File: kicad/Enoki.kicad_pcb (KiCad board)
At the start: 2 copper layers, 40 x 23 mm, 16 parts, among them J1 Conn_01x08_Male

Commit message: save
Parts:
- DS1: footprint Display:OLED-128O064D -> allen-synthesis:KH-FPC0.5-H2.0SMT-30P-QCH FPC Connector 30 pin
- R4: value 390K -> 330K
- moved DS1 4.60 mm to (137.2, 158.8), turned to 0 degrees
- moved C3 0.80 mm to (126.7, 151.4)
- moved C1 0.76 mm to (128.8, 149.0)
- moved C2 0.70 mm to (145.4, 149.0)
- moved C4 0.70 mm to (147.3, 151.4)
- moved C5 0.70 mm to (143.3, 151.4)
- moved R1 0.64 mm to (140.3, 150.2)
- moved C6 0.63 mm to (130.8, 151.4)
- moved R4 0.63 mm to (133.9, 150.2)
- moved JP1 0.38 mm to (151.1, 151.1)
- moved R3 0.25 mm to (136.0, 150.2)
- moved R2 0.13 mm to (138.2, 150.2)
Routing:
- net GND: track 28.0 -> 15.0 mm, vias 6 -> 8
- net /D0/SCLK/SCK_3.3V: track 21.3 -> 13.1 mm, vias 2 -> 0
- net +3V3: track 53.5 -> 60.3 mm, vias 3 -> 2
- net /RST_3.3V: track 8.62 -> 14.4 mm
- net Net-(DS1-C2N): track 3.22 -> 6.56 mm
- net Net-(DS1-VCC): track 2.86 -> 5.65 mm
- net Net-(DS1-C2P): track 2.86 -> 5.55 mm
- net Net-(DS1-D2): track 27.7 -> 25.1 mm, vias 0 -> 2
- net /CS_3.3V: track 10.2 -> 12.4 mm, vias 2 -> 0
- net Net-(DS1-VCOMH): track 3.40 -> 4.96 mm
- net Net-(DS1-C1P): track 3.44 -> 4.88 mm
- net Net-(DS1-BS1): track 14.5 -> 15.8 mm
- net Net-(DS1-IREF): track 6.78 -> 5.44 mm
- net /D1/MOSI/SDA_3.3V: track 40.4 -> 41.4 mm
- net /DC/SA0_3.3V: track 15.3 -> 16.2 mm
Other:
- board text removed: "stay silly"

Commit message: save
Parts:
- removed REF**: PinHeader_1x02_P2.54mm_Vertical_SMD_Pin1Left, Connector_PinHeader_2.54mm:PinHeader_1x02_P2.54mm_Vertical_SMD_Pin1Left
- removed REF**: PinHeader_1x02_P2.54mm_Vertical_SMD_Pin1Right, Connector_PinHeader_2.54mm:PinHeader_1x02_P2.54mm_Vertical_SMD_Pin1Right
- added J2: Conn_01x02_Pin, Connector_PinHeader_2.54mm:PinHeader_1x02_P2.54mm_Vertical_SMD_Pin1Right, F.Cu at (120.7, 160.8)
- added J3: Conn_01x02_Pin, Connector_PinHeader_2.54mm:PinHeader_1x02_P2.54mm_Vertical_SMD_Pin1Right, F.Cu at (153.7, 160.8)

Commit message: save
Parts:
- moved J3 183.5 mm to (35.6, 20.3)
- moved C1 183.1 mm to (11.7, 8.28)
- moved C2 183.1 mm to (28.3, 8.28)
- moved DS1 183.1 mm to (20.1, 18.1)
- moved JP1 183.1 mm to (34.0, 10.4)
- moved JP2 183.1 mm to (37.8, 10.4)
- moved R1 183.1 mm to (23.2, 9.53)
- moved R2 183.1 mm to (21.1, 9.53)
- moved R3 183.1 mm to (18.9, 9.53)
- moved R4 183.1 mm to (16.8, 9.53)
- moved C3 183.1 mm to (9.65, 10.7)
- moved C4 183.1 mm to (30.2, 10.7)
- moved C5 183.1 mm to (26.2, 10.7)
- moved C6 183.1 mm to (13.7, 10.7)
- moved J1 182.8 mm to (20.3, 3.81)
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
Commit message: save
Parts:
- JP1, JP2: footprint Jumper:SolderJumper-2_P1.3mm_Open_RoundedPad1.0x1.5mm -> Jumper:SolderJumper-2_P1.3mm_Bridged_RoundedPad1.0x1.5mm
- moved J3 1.27 mm to (36.8, 20.3)
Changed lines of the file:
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@@
     )
   )
-  (footprint "Jumper:SolderJumper-2_P1.3mm_Open_RoundedPad1.0x1.5mm" (layer "F.Cu")
+  (footprint "Jumper:SolderJumper-2_P1.3mm_Bridged_RoundedPad1.0x1.5mm" (layer "F.Cu")
     (at 34.036 10.414)
-    (descr "SMD Solder Jumper, 1x1.5mm, rounded Pads, 0.3mm gap, open")
-    (tags "solder jumper open")
+    (descr "SMD Solder Jumper, 1x1.5mm, rounded Pads, 0.3mm gap, bridged with 1 copper strip")
+    (tags "net tie solder jumper bridged")
     (property "Sheetfile" "Enoki.kicad_sch")
     (property "Sheetname" "")
@@
     (property "ki_keywords" "solder jumper SPST")
     (attr exclude_from_pos_files)
-    (fp_text reference "JP1" (at 0 -1.778) (layer "F.SilkS")
-        (effects (font (size 0.5 0.5) (thickness 0.075)))
+    (net_tie_pad_groups "1, 2")
+    (fp_text reference "JP1" (at 0 -1.8) (layer "F.SilkS")
+        (effects (font (size 1 1) (thickness 0.15)))
     )
     (fp_text value "Close for I2C" (at 0 1.9) (layer "F.Fab")
         (effects (font (size 1 1) (thickness 0.15)))
     )
+    (fp_poly
+      (pts
+        (xy 0.25 -0.3)
+        (xy -0.25 -0.3)
+        (xy -0.25 0.3)
+        (xy 0.25 0.3)
+      )
+      (stroke (width 0) (type solid)) (fill solid) (layer "F.Cu"))
     (fp_line (start -1.4 0.3) (end -1.4 -0.3)
       (stroke (width 0.12) (type solid)) (layer "F.SilkS"))
@@
       ))
   )
-  (footprint "Jumper:SolderJumper-2_P1.3mm_Open_RoundedPad1.0x1.5mm" (layer "F.Cu")
+  (footprint "Jumper:SolderJumper-2_P1.3mm_Bridged_RoundedPad1.0x1.5mm" (layer "F.Cu")
     (at 37.846 10.414)
-    (descr "SMD Solder Jumper, 1x1.5mm, rounded Pads, 0.3mm gap, open")
-    (tags "solder jumper open")
+    (descr "SMD Solder Jumper, 1x1.5mm, rounded Pads, 0.3mm gap, bridged with 1 copper strip")
+    (tags "net tie solder jumper bridged")
     (property "Sheetfile" "Enoki.kicad_sch")
     (property "Sheetname" "")
@@
     (property "ki_keywords" "solder jumper SPST")
     (attr exclude_from_pos_files)
+    (net_tie_pad_groups "1, 2")
     (fp_text reference "JP2" (at 0 -1.8) (layer "F.SilkS")
-        (effects (font (size 0.5 0.5) (thickness 0.075)))
+        (effects (font (size 1 1) (thickness 0.15)))
     )
     (fp_text value "Close for I2C" (at 0 1.9) (layer "F.Fab")
         (effects (font (size 1 1) (thickness 0.15)))
     )
+    (fp_poly
+      (pts
+        (xy 0.25 -0.3)
+        (xy -0.25 -0.3)
+        (xy -0.25 0.3)
+        (xy 0.25 0.3)
+      )
+      (stroke (width 0) (type solid)) (fill solid) (layer "F.Cu"))
     (fp_line (start -1.4 0.3) (end -1.4 -0.3)
       (stroke (width 0.12) (type solid)) (layer "F.SilkS"))
@@
   )
   (footprint "Connector_PinHeader_2.54mm:PinHeader_1x02_P2.54mm_Vertical_SMD_Pin1Right" (layer "F.Cu")
-    (at 35.56 20.32)
+    (at 36.83 20.32)
     (descr "surface-mounted straight pin header, 1x02, 2.54mm pitch, single row, style 2 (pin 1 right)")
     (tags "Surface mounted pin header SMD 1x02 2.54mm single row style2 pin1 right")
@@
   (gr_line (start 137.16 161.671) (end 137.16 138.557)
     (stroke (width 0.15) (type solid)) (layer "Dwgs.User"))
-  (gr_rect (start 0 0) (end 40 23)
+  (gr_rect (start 0.32 0) (end 40.32 23)
     (stroke (width 0.1) (type solid)) (fill none) (layer "Edge.Cuts"))
   (image (at -32.004 53.34) (layer "User.2") (scale 0.162064)
@@
     (polygon
       (pts
-        (xy 40.005 23.114)
-        (xy 0 22.987)
-        (xy 0 0)
-        (xy 40.005 0)
+        (xy 40.325 23.114)
+        (xy 0.32 22.987)
+        (xy 0.32 0)
+        (xy 40.325 0)
       )
     )

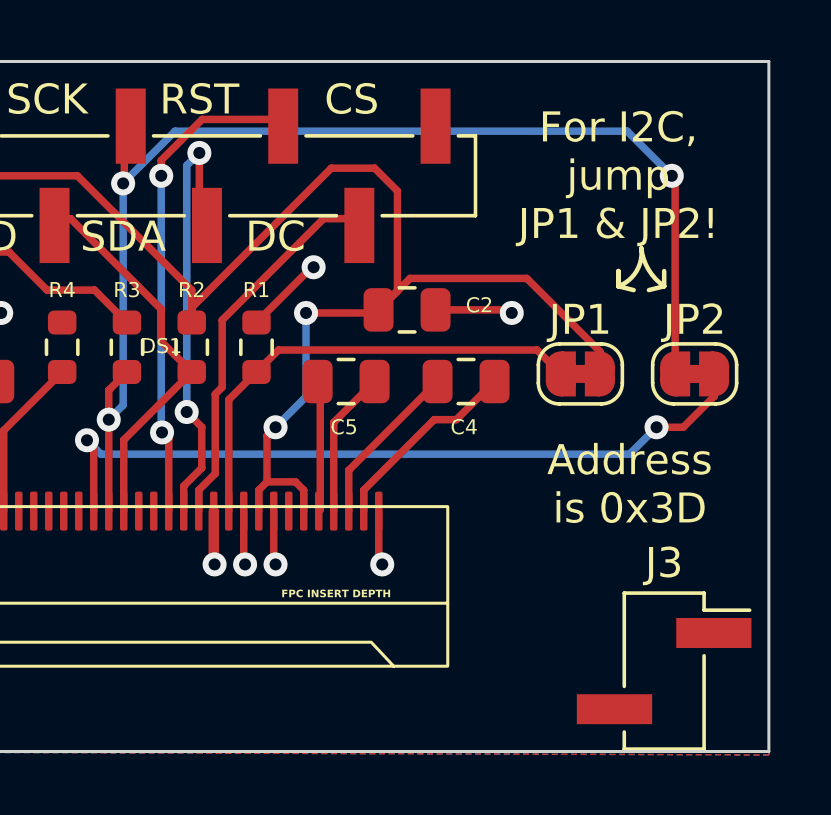
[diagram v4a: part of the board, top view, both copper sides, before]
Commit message: update pcb
I2C jumpers are now closed by default
RC circuit added to RST pin to remove need for manual triggering by MCU on power up
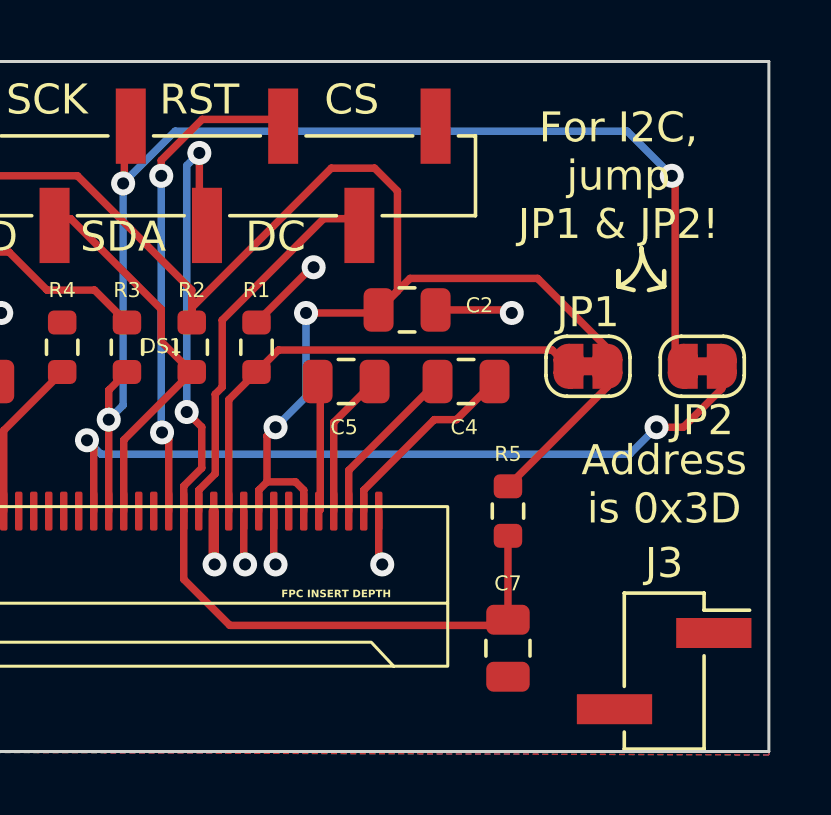
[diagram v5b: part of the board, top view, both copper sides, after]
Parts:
- added C7: 2.2uF, Capacitor_SMD:C_0805_2012Metric, F.Cu at (31.6, 19.6)
- added R5: 10K, Resistor_SMD:R_0603_1608Metric, F.Cu at (31.6, 15.0)
- JP1, JP2: value Close for I2C -> Cut for SPI
- moved JP2 0.36 mm to (38.1, 10.2), turned to 180 degrees
- moved JP1 0.36 mm to (34.3, 10.2)
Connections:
- JP2 pad 1: /D1/MOSI/SDA_3.3V -> Net-(DS1-D2)
- JP2 pad 2: Net-(DS1-D2) -> /D1/MOSI/SDA_3.3V
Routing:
- net /RST_3.3V: track 14.8 -> 31.4 mm
- net +3V3: track 60.6 -> 66.1 mm
